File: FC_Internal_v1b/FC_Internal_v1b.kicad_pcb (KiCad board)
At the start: 4 copper layers, 88 x 94.5 mm, 103 parts, among them IC1 RP2040_QFN56, IC2 AZ1117CH-3.3TRG1, J1 Conn_ARM_JTAG_SWD_10, J10 BM04B-SRSS-TB(LF)(SN), J11 BM04B-SRSS-TB(LF)(SN), J12 BM04B-SRSS-TB(LF)(SN), J13 Breakout, J14 Battery, J15 Breakout, J2 FC to EPS Connector, J3 DNI, J4 104031-0811, J5 BM04B-SRSS-TB(LF)(SN), J6 Conn_Coaxial, J7 Breakout, J8 USB_B_Micro, J9 BM04B-SRSS-TB(LF)(SN), SW1 KMR2, SW2 KMR2, U10 AP3602AKTR-G1, U3 MAX706RESA, U4 RFM98PW, U5 RFM9xBreakout, U6 W25Q128JV, U7 LSM6DSOTR, U8 LSM303AGRTR, U9 MCP25625-E/ML, Y1 12MHZ, Y3 16MHZ 12 pf

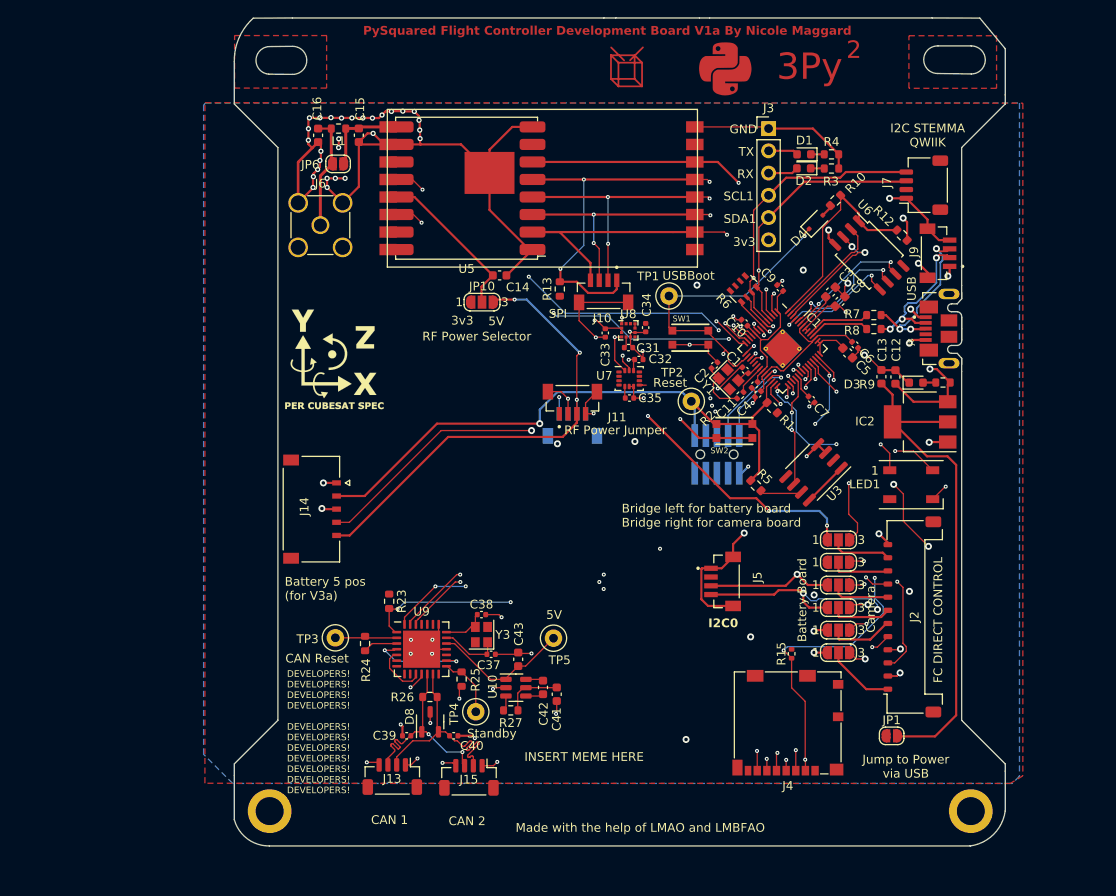
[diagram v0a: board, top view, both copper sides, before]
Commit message: Nudged flash chip to make space
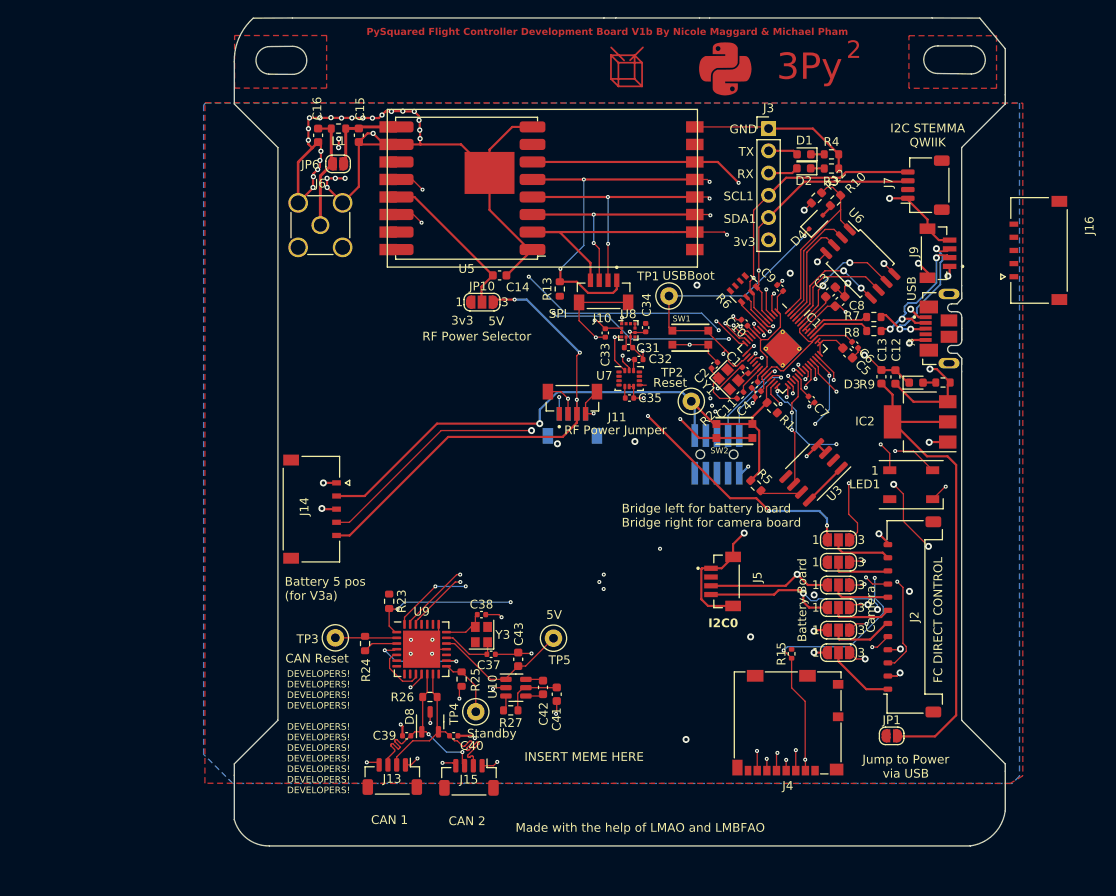
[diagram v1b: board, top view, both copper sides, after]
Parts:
- removed ? (x2): , 
- removed REF**: Val**, mainboard:XYZ_cubesat-top
- added J16: Debug, FC_DEV_BOARD:MOLEX_5040500591, F.Cu at (235.2, 74.1)
- J3: value DNI -> Life Makes Lemonade
- moved R12 10.6 mm to (209.8, 68.1), turned to 45 degrees
- moved U6 1.39 mm to (214.8, 75.6)
- moved R8 0.23 mm to (216.3, 83.3)
- moved R7 0.22 mm to (216.3, 81.7)
- moved J7 0.17 mm to (222.2, 66.7)
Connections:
- net /D+ renamed D+
- net /D- renamed D-
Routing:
- net /QSPI_CS: track 24.4 -> 21.3 mm
- net /QSPI_DATA[2]: track 14.6 -> 12.1 mm, vias 2 -> 0
- net /QSPI_SCK: track 15.3 -> 13.2 mm, vias 2 -> 0
- net /QSPI_DATA[0]: track 14.7 -> 13.4 mm
- net GND: track 249.1 -> 248.6 mm
- net 3.3V: track 64.2 -> 64.3 mm, vias 15 -> 16
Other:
- board text added: "PySquared Flight Controller Development Board V1b By Nicole Maggard & Michael Pham"
- board text removed: "PySquared Flight Controller Development Board V1a By Nicole Maggard"

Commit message: Added 5pos Debug Connector to Layout
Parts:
- J7: footprint Connector_JST:JST_SH_SM04B-SRSS-TB_1x04-1MP_P1.00mm_Horizontal -> FC_DEV_BOARD:JST_BM04B-SRSS-TB(LF)(SN)
- moved J16 16.7 mm to (222.5, 63.3)
- moved J7 8.04 mm to (214.2, 66.1)
- moved R10 1.47 mm to (211.0, 69.5)
- moved D4 1.33 mm to (208.8, 71.8)
- moved R12 0.32 mm to (209.9, 68.4)
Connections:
- IC1 pad 46: D- -> /D-
- IC1 pad 47: D+ -> /D+
- J16 pad 3: D+ -> USB_D+
- J16 pad 4: D- -> USB_D-
- R7 pad 1: D+ -> /D+
- R8 pad 1: D- -> /D-
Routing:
- net FC_RESET: track 71.9 -> 131.3 mm, vias 1 -> 3
- net D3: track 79.1 -> 96.8 mm, vias 3 -> 5
- net USB_D-: track 18.5 -> 34.7 mm
- net GND: track 248.6 -> 264.4 mm, vias 73 -> 84
- net USB_D+: track 19.3 -> 33.0 mm
- net /QSPI_CS: track 21.3 -> 12.8 mm
- net D+: track 7.33 -> 0.00 mm
- net /D+: track 0.00 -> 7.33 mm
- net D-: track 6.98 -> 0.00 mm
- net /D-: track 0.00 -> 6.98 mm
- net SDA1: track 55.5 -> 52.4 mm
- net SCL1: track 58.0 -> 54.9 mm

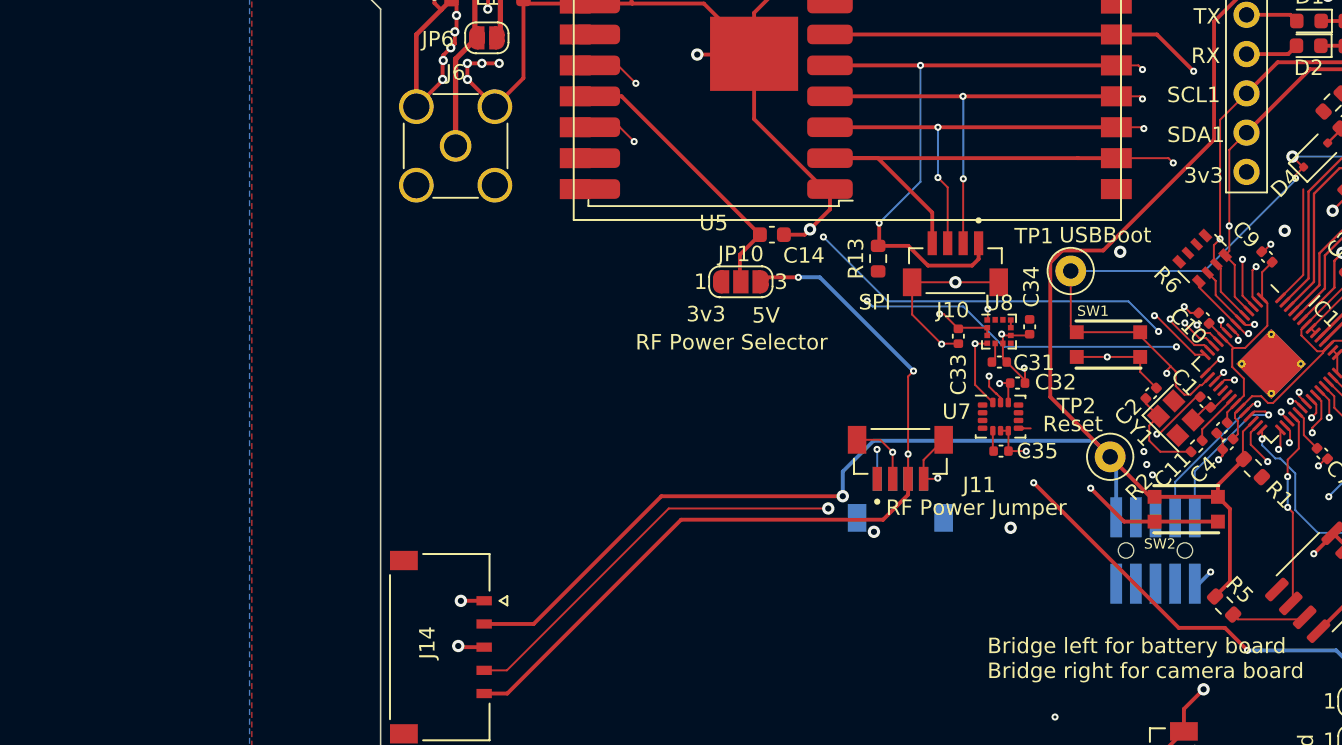
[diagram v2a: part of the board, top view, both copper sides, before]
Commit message: Finished Schematic Capture for New SD Card Holder
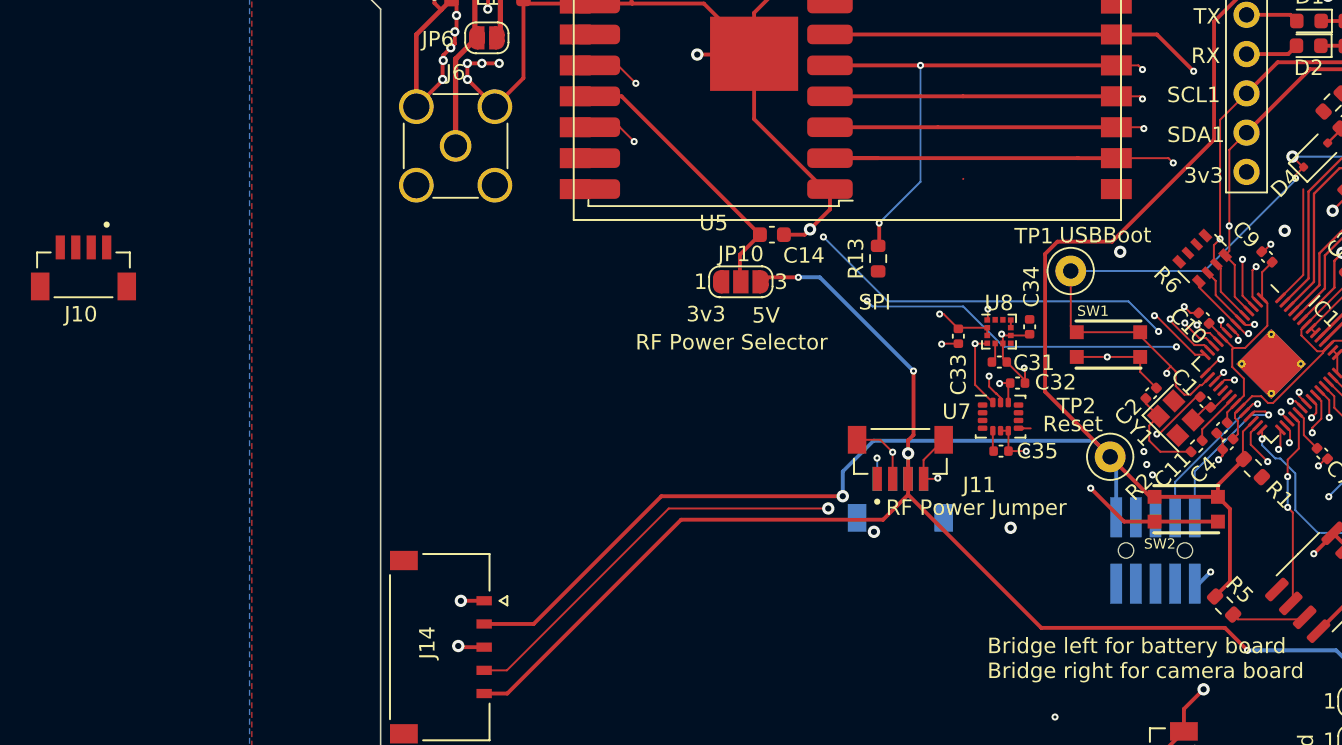
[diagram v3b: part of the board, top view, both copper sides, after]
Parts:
- moved J10 56.4 mm to (129.1, 80.3)
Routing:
- net GND: track 264.4 -> 254.0 mm, vias 84 -> 83
- net SPI0_SCK: track 139.9 -> 130.4 mm, vias 8 -> 6
- net SPI0_CS0: track 61.5 -> 53.3 mm
- net SPI0_MOSI: track 138.5 -> 130.7 mm, vias 8 -> 6
- net SPI0_MISO: track 134.9 -> 127.9 mm
- net VCC_RF1: track 93.5 -> 90.6 mm, vias 6 -> 5
- net FC_RESET: track 131.3 -> 132.1 mm
- net 3.3V: track 64.8 -> 64.2 mm

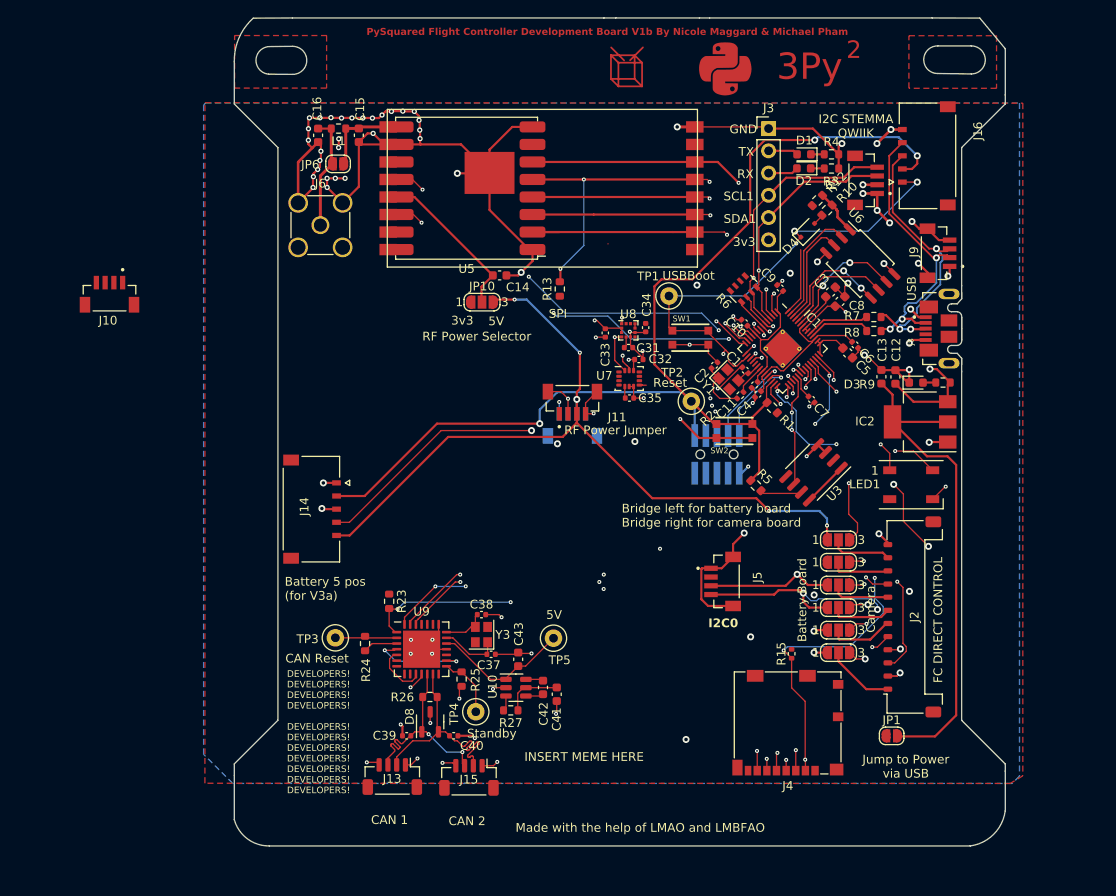
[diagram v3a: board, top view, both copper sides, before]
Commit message: Finished Adding SD Card To Layout
Also moved the SD card to more convenient slot
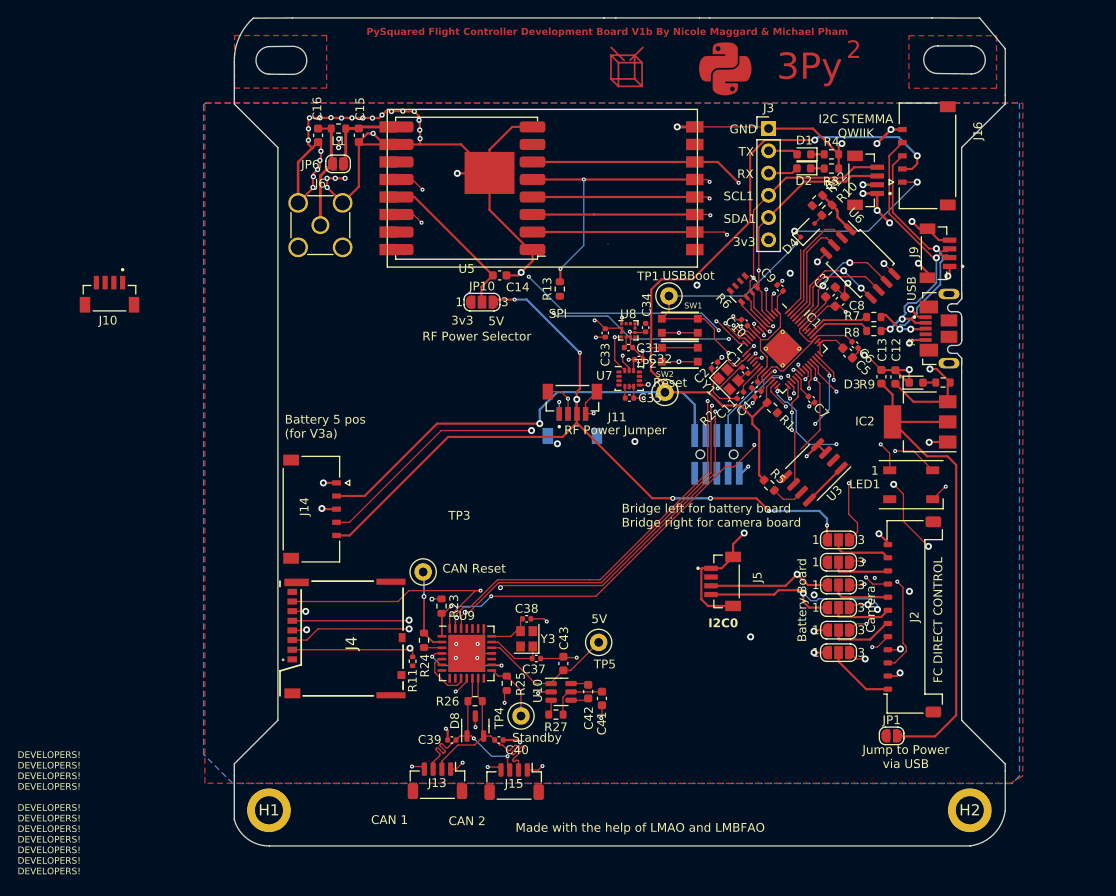
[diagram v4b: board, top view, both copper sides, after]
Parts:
- removed R15: 10k, Resistor_SMD:R_0402_1005Metric
- added H1: MountingHole, , F.Cu at (147.3, 138.0)
- added H2: MountingHole, , F.Cu at (227.3, 138.0)
- added R11: 10k, Resistor_SMD:R_0402_1005Metric, F.Cu at (163.7, 121.0)
- J4: value 104031-0811 -> Molex 503398-1892; footprint Connector_Card:microSD_HC_Molex_104031-0811 -> Molex 503398-1892:503398-1892-1
- moved J4 58.1 mm to (148.6, 124.9), turned to 90 degrees
- moved TP3 12.5 mm to (164.9, 110.8)
- moved SW2 10.7 mm to (194.2, 86.0)
- moved R24 6.74 mm to (165.0, 118.6)
- moved R23 6.01 mm to (167.0, 114.7)
- moved C40 5.18 mm to (173.5, 130.0)
- moved C37 5.18 mm to (177.8, 120.7)
- moved C38 5.18 mm to (176.7, 116.2)
- moved C43 5.18 mm to (180.9, 121.2)
- moved R25 5.18 mm to (174.4, 123.5)
- moved R26 5.18 mm to (170.8, 125.5)
- moved R27 5.18 mm to (180.1, 127.1)
- moved TP5 5.18 mm to (184.9, 118.8)
- moved Y3 5.18 mm to (176.7, 118.4)
- moved C39 5.18 mm to (168.2, 130.0)
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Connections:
- J4 pad 10: (no net) -> unconnected-(J4-DETECT_SWITCH-Pad10)
- J4 pad 9: (no net) -> unconnected-(J4-DETECT_LEVER-Pad9)
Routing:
- net SPI0_MOSI: track 130.7 -> 113.9 mm, vias 6 -> 5
- net SPI0_SCK: track 130.4 -> 115.1 mm, vias 6 -> 5
- net SPI0_MISO: track 127.9 -> 116.8 mm, vias 7 -> 5
- net SPI0_CS2: track 71.0 -> 63.2 mm
- net FC_RESET: track 132.1 -> 138.4 mm
- net GND: track 254.0 -> 247.7 mm, vias 83 -> 84
- net Net-(U9-RESET): track 6.99 -> 9.48 mm, vias 0 -> 1
- net Net-(U3-~{RESET}): track 5.09 -> 4.14 mm
- net TXCAN: track 11.0 -> 10.5 mm
- net 3.3V: track 64.2 -> 64.0 mm, vias 16 -> 17
- net SPI0_CS1: track 59.8 -> 59.9 mm, vias 4 -> 3
- net VCC_RF1: vias 5 -> 7
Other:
- board text removed: "INSERT MEME HERE"

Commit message: Finished First Pass Retracing
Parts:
- moved J10 32.6 mm to (161.7, 80.9)
- moved J5 27.8 mm to (216.0, 89.0)
- moved R5 7.84 mm to (203.6, 93.1)
- moved C13 6.05 mm to (216.3, 94.5), turned to -90 degrees
- moved U3 3.10 mm to (208.0, 96.7), turned to 135 degrees
- moved TP1 3.04 mm to (196.0, 79.2)
- moved C5 3.01 mm to (211.7, 83.2), turned to 180 degrees
- moved C6 1.30 mm to (213.4, 84.5), turned to 0 degrees
- moved C7 1.23 mm to (209.0, 89.9)
- moved R13 0.14 mm to (180.5, 78.6)
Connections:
- IC1 pad 19: unconnected-(IC1-TESTEN-Pad19) -> GND
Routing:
- net SDA0: track 71.3 -> 45.3 mm
- net SCL0: track 71.9 -> 48.3 mm
- net SPI0_CS1: track 59.9 -> 77.9 mm, vias 3 -> 4
- net 3.3V: track 64.0 -> 77.0 mm, vias 17 -> 25
- net FC_RESET: track 138.4 -> 128.4 mm, vias 3 -> 5
- net /QSPI_CS: track 12.8 -> 18.6 mm
- net GND: track 247.7 -> 242.8 mm, vias 84 -> 86
- net HS: track 50.2 -> 46.1 mm, vias 4 -> 0
- net D3: track 97.2 -> 93.2 mm
- net ENAB_RF / D2: track 45.8 -> 49.6 mm, vias 2 -> 4
- net WDT_WDI: track 12.7 -> 9.43 mm
- net D7: track 30.9 -> 33.8 mm, vias 3 -> 1
- net 1.2V: track 22.4 -> 19.7 mm
- net /3v3 Spec: track 57.3 -> 54.6 mm
- net BURN_RELAY_A / D5: track 37.2 -> 39.8 mm, vias 2 -> 4
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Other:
- board text added: "PySquared Flight Controller Board V4 By Nicole Maggard & Michael Pham"
- board text added: "RST"
- board text removed: "PySquared Flight Controller Development Board V1b By Nicole Maggard & Michael Pham"
- board text removed: "Reset"
